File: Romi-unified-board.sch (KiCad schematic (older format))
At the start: 74 parts, among them J1 ServoAnalog, J10 LIDAR_DATA, J11 LIDAR_MOTOR, J12 ROMI-Encoder, J13 ROMI-Encoder, J14 THING, J15 THING, J16 Conn_01x03_Male, J17 Conn_01x03_Male, J18 Conn_01x03_Male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

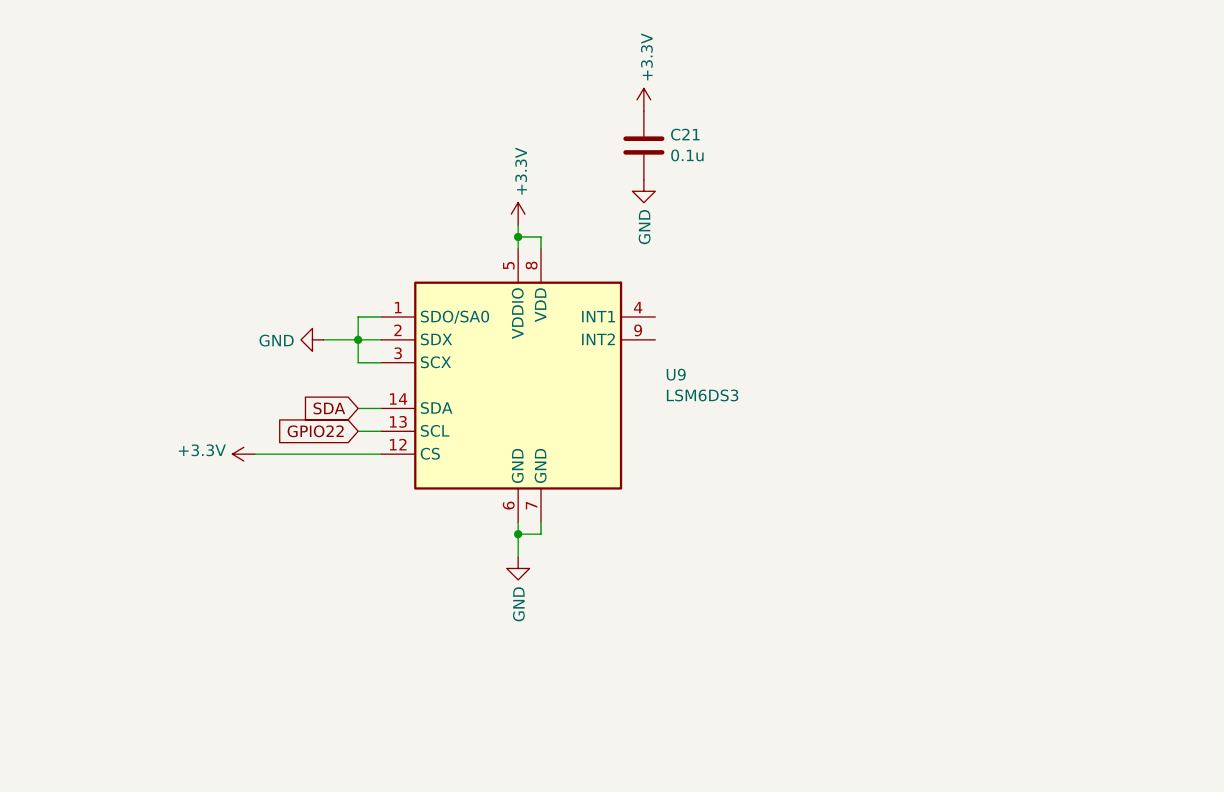
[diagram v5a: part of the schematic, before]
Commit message: More rev2 changes
Fixed inductor FP
Swapped out accelerometer with an in stock variant.
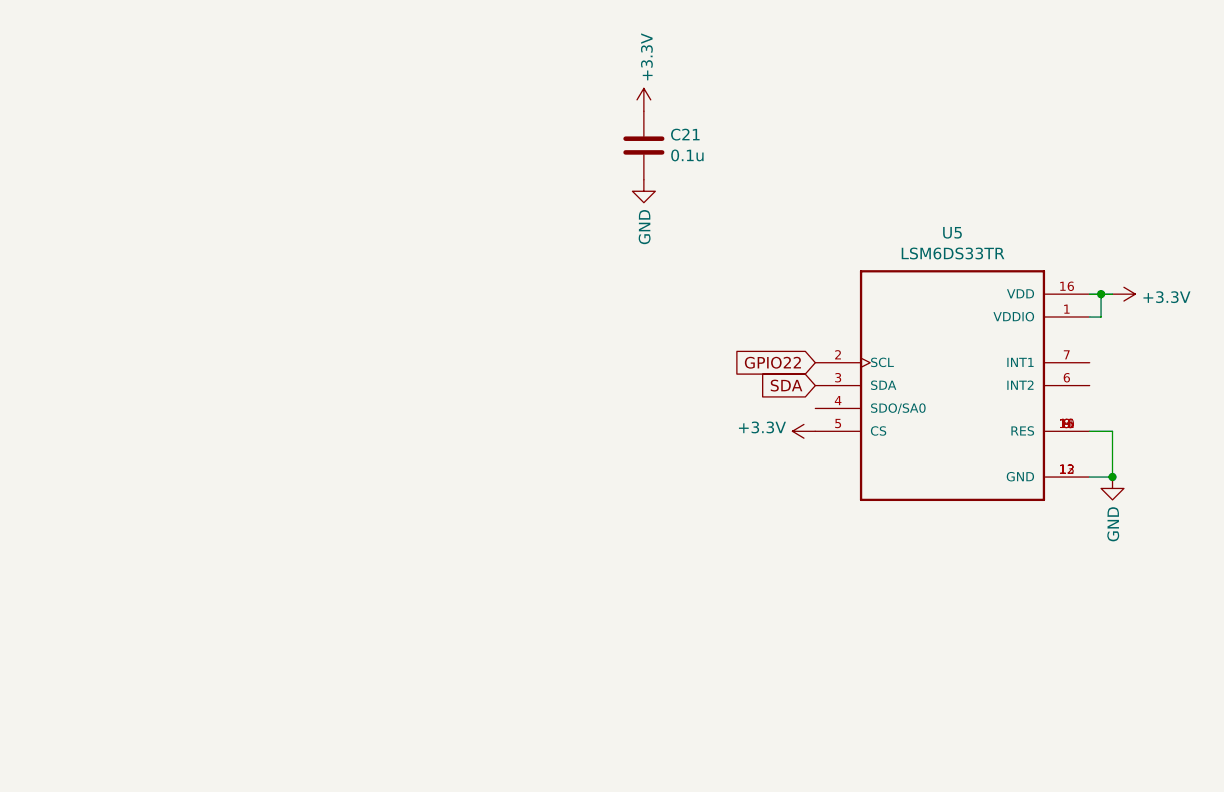
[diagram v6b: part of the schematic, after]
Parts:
- removed U9: LSM6DS3, Package_LGA:LGA-14_3x2.5mm_P0.5mm_LayoutBorder3x4y, symbol Sensor_Motion:LSM6DS3
- added U5: LSM6DS33TR, unified:PQFN50P300X300X86-16N, symbol LSM6DS33TR:LSM6DS33TR
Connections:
- wire segments 279 -> 269
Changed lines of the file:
@@
 SDA
-$Comp
-L Sensor_Motion:LSM6DS3 U9
-U 1 1 5FAEECB9
-P 17650 -1750
-F 0 "U9" H 18294 -1704 50  0000 L CNN
-F 1 "LSM6DS3" H 18294 -1795 50  0000 L CNN
-F 2 "Package_LGA:LGA-14_3x2.5mm_P0.5mm_LayoutBorder3x4y" H 17250 -2450 50  0001 L CNN
-F 3 "www.st.com/resource/en/datasheet/lsm6ds3.pdf" H 17750 -2400 50  0001 C CNN
-	1    17650 -1750
-	1    0    0    -1
-$EndComp
 $Comp
 L power:GND #PWR0172
 U 1 1 5FAEFB38
-P 17650 -1000
-F 0 "#PWR0172" H 17650 -1250 50  0001 C CNN
-F 1 "GND" V 17655 -1128 50  0000 R CNN
-F 2 "" H 17650 -1000 50  0001 C CNN
-F 3 "" H 17650 -1000 50  0001 C CNN
-	1    17650 -1000
+P 20250 -1350
+F 0 "#PWR0172" H 20250 -1600 50  0001 C CNN
+F 1 "GND" V 20255 -1478 50  0000 R CNN
+F 2 "" H 20250 -1350 50  0001 C CNN
+F 3 "" H 20250 -1350 50  0001 C CNN
+	1    20250 -1350
 	1    0    0    -1
 $EndComp
@@
 L power:+3.3V #PWR0173
 U 1 1 5FAEFF10
-P 17650 -2450
-F 0 "#PWR0173" H 17650 -2600 50  0001 C CNN
-F 1 "+3.3V" V 17665 -2322 50  0000 L CNN
-F 2 "" H 17650 -2450 50  0001 C CNN
-F 3 "" H 17650 -2450 50  0001 C CNN
-	1    17650 -2450
-	1    0    0    -1
-$EndComp
-Wire Wire Line
-	17650 -2450 17650 -2400
-Wire Wire Line
-	17650 -2400 17750 -2400
-Wire Wire Line
-	17750 -2400 17750 -2350
-Connection ~ 17650 -2400
-Wire Wire Line
-	17650 -2400 17650 -2350
-Wire Wire Line
-	17650 -1150 17650 -1100
-Wire Wire Line
-	17650 -1100 17750 -1100
-Wire Wire Line
-	17750 -1100 17750 -1150
-Connection ~ 17650 -1100
-Wire Wire Line
-	17650 -1100 17650 -1000
-Text GLabel 16950 -1650 0    50   Input ~ 0
+P 20250 -2150
+F 0 "#PWR0173" H 20250 -2300 50  0001 C CNN
+F 1 "+3.3V" V 20265 -2022 50  0000 L CNN
+F 2 "" H 20250 -2150 50  0001 C CNN
+F 3 "" H 20250 -2150 50  0001 C CNN
+	1    20250 -2150
+	0    1    1    0
+$EndComp
+Text GLabel 18950 -1750 0    50   Input ~ 0
 SDA
-Text GLabel 16950 -1550 0    50   Input ~ 0
+Text GLabel 18950 -1850 0    50   Input ~ 0
 GPIO22
-Wire Wire Line
-	17050 -1650 16950 -1650
-Wire Wire Line
-	16950 -1550 17050 -1550
-Wire Wire Line
-	17050 -1450 16500 -1450
 $Comp
 L power:+3.3V #PWR0174
 U 1 1 5FC03884
-P 16500 -1450
-F 0 "#PWR0174" H 16500 -1600 50  0001 C CNN
-F 1 "+3.3V" V 16515 -1322 50  0000 L CNN
-F 2 "" H 16500 -1450 50  0001 C CNN
-F 3 "" H 16500 -1450 50  0001 C CNN
-	1    16500 -1450
-	0    -1   -1   0
-$EndComp
-$Comp
-L power:GND #PWR0175
-U 1 1 5FC0529D
-P 16800 -1950
-F 0 "#PWR0175" H 16800 -2200 50  0001 C CNN
-F 1 "GND" V 16805 -2078 50  0000 R CNN
-F 2 "" H 16800 -1950 50  0001 C CNN
-F 3 "" H 16800 -1950 50  0001 C CNN
-	1    16800 -1950
-	0    1    1    0
-$EndComp
-Wire Wire Line
-	17050 -1950 16950 -1950
-Wire Wire Line
-	17050 -1850 16950 -1850
-Wire Wire Line
-	16950 -1850 16950 -1950
-Connection ~ 16950 -1950
-Wire Wire Line
-	16950 -1950 16800 -1950
-Wire Wire Line
-	17050 -2050 16950 -2050
-Wire Wire Line
-	16950 -2050 16950 -1950
+P 18950 -1550
+F 0 "#PWR0174" H 18950 -1700 50  0001 C CNN
+F 1 "+3.3V" V 18965 -1422 50  0000 L CNN
+F 2 "" H 18950 -1550 50  0001 C CNN
+F 3 "" H 18950 -1550 50  0001 C CNN
+	1    18950 -1550
+	0    -1   -1   0
+$EndComp
 $Comp
 L Device:C C21
@@
 Wire Wire Line
 	2750 -450 2600 -450
+$Comp
+L LSM6DS33TR:LSM6DS33TR U5
+U 1 1 5FA8D316
+P 19550 -1750
+F 0 "U5" H 19550 -1083 50  0000 C CNN
+F 1 "LSM6DS33TR" H 19550 -1174 50  0000 C CNN
+F 2 "unified:PQFN50P300X300X86-16N" H 19550 -1750 50  0001 L BNN
+F 3 "6" H 19550 -1750 50  0001 L BNN
+F 4 "STMicroelectronics" H 19550 -1750 50  0001 L BNN "Field4"
+F 5 "IPC-7351B" H 19550 -1750 50  0001 L BNN "Field5"
+	1    19550 -1750
+	1    0    0    -1
+$EndComp
+Wire Wire Line
+	20250 -2150 20200 -2150
+Wire Wire Line
+	20150 -2050 20200 -2050
+Wire Wire Line
+	20200 -2050 20200 -2150
+Connection ~ 20200 -2150
+Wire Wire Line
+	20200 -2150 20150 -2150
+Wire Wire Line
+	20150 -1550 20250 -1550
+Wire Wire Line
+	20250 -1550 20250 -1350
+Wire Wire Line
+	20150 -1350 20250 -1350
+Connection ~ 20250 -1350
 $EndSCHEMATC
